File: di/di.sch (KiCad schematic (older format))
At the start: 35 parts

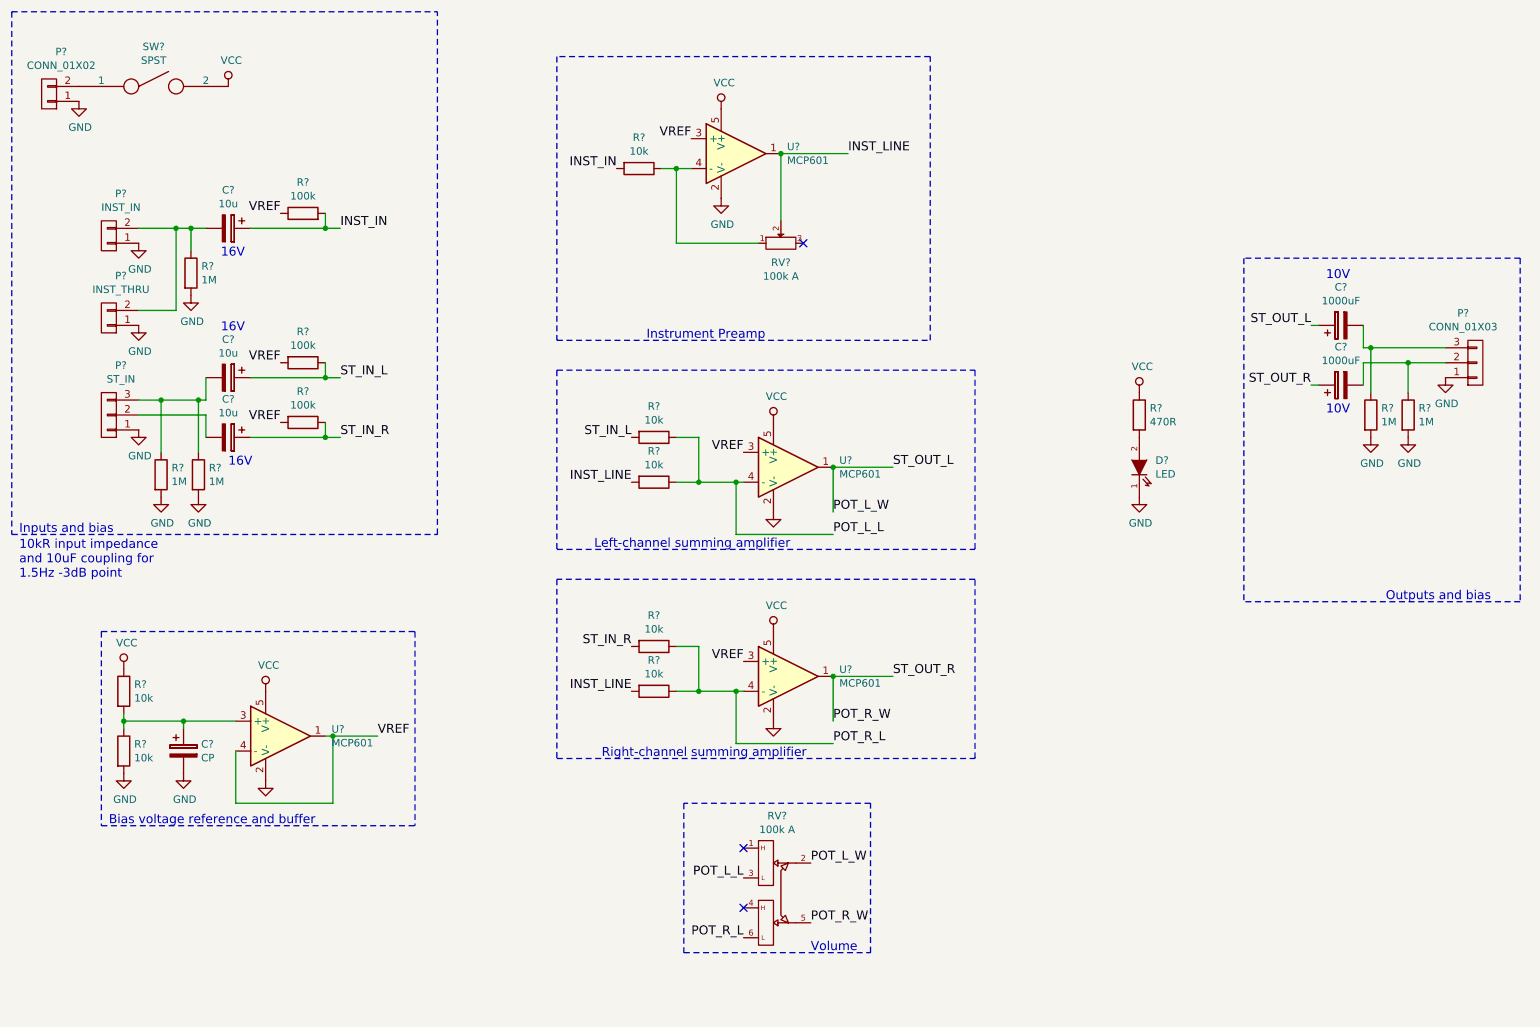
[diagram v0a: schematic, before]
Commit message: Higher impedance inst inputs
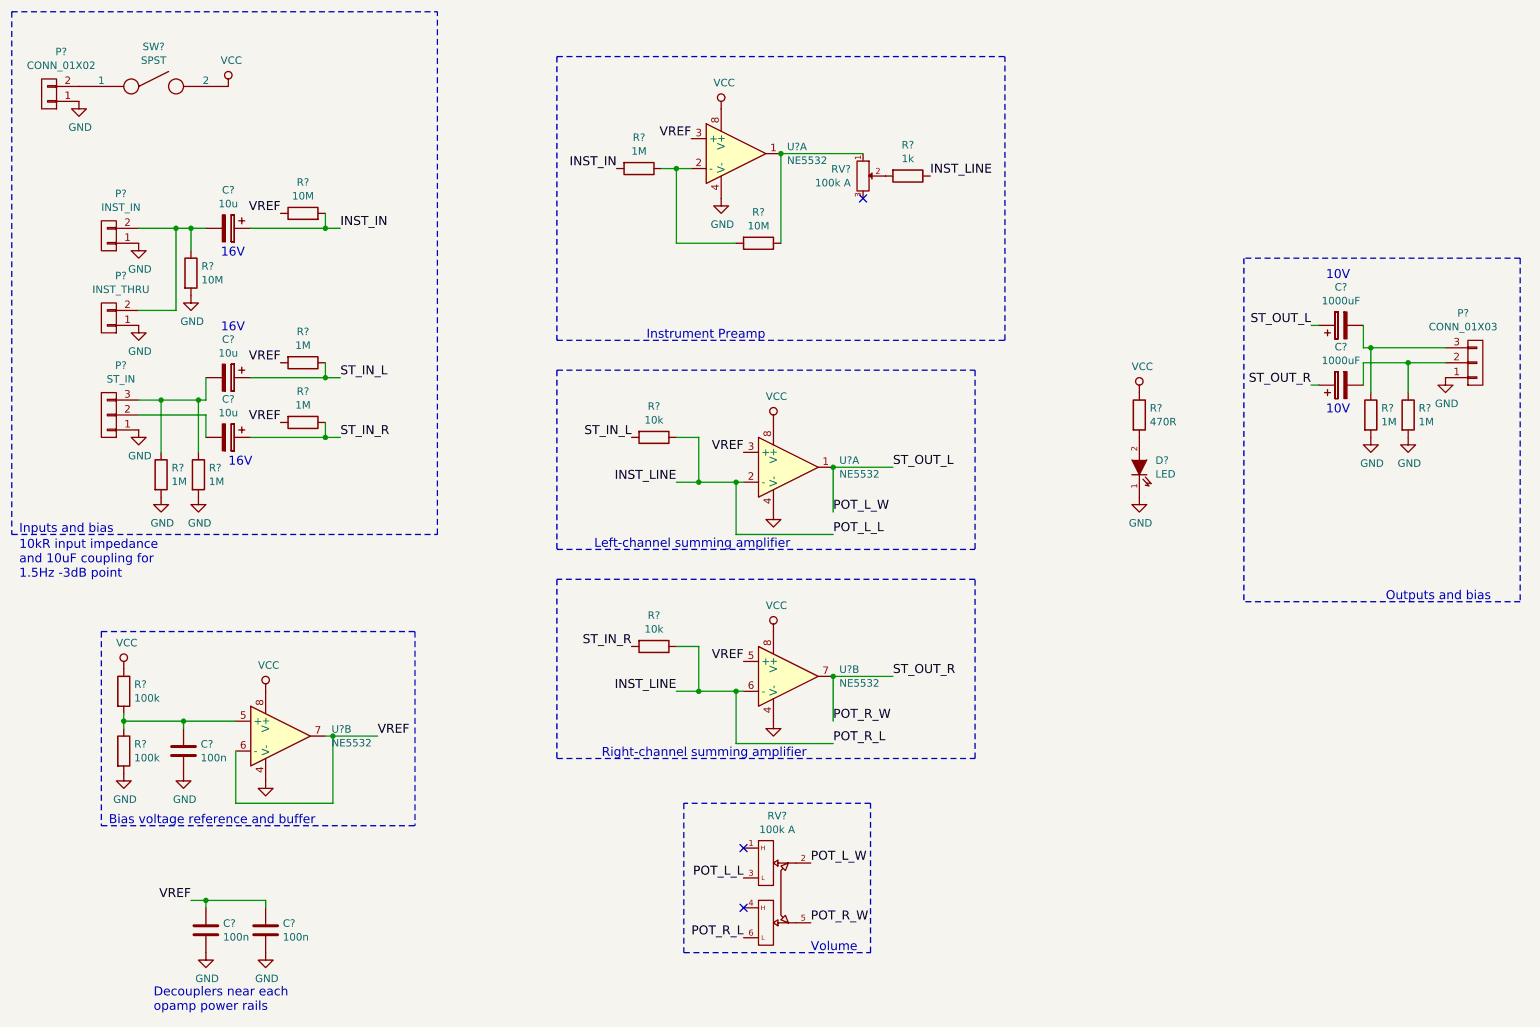
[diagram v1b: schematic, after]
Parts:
- removed C?: CP, symbol CP
- removed R? (x2): 10k, symbol R
- removed RV?: 100k A, symbol POT
- removed U? (x4): MCP601, symbol MCP601
- added C? (x3): 100n, symbol C
- added R?: 10M, symbol R
- added R?: 1k, symbol R
- added RV?: 100k A, symbol POT
- added U? (x4): NE5532, symbol NE5532
- R?: value 10k -> 1M
- R? (x2): value 10k -> 100k
- R?: value 100k -> 10M
- R? (x2): value 100k -> 1M
- R?: value 1M -> 10M
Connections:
- net POT_L_L is gone; now on net INST_LINE: R?.1, RV?.3
- net POT_R_L is gone; now on net INST_LINE: R?.1, RV?.6
- net GND: now also C?.2, C?.2, C?.2, U?.4 (V-), U?.4 (V-), U?.4 (V-), U?.4 (V-)
- net INST_LINE: now also R?.1, U?.2 (-), U?.6 (-)
- net POT_L_W: now also U?.1
- net POT_R_W: now also U?.7
- net VCC: now also U?.8 (V+), U?.8 (V+), U?.8 (V+), U?.8 (V+)
- net VREF: now also C?.1, C?.1, U?.3 (+), U?.3 (+), U?.5 (+), U?.6 (-), U?.7
- net at R?.1: now also R?.2, U?.2 (-)
- net at R?.1, R?.2: now also C?.1, U?.5 (+)
- new net: R?.1, RV?.1, U?.1
- new net: R?.2, RV?.2
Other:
- note added: "Decouplers near each\nopamp power rails"

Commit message: removed coupling from DI
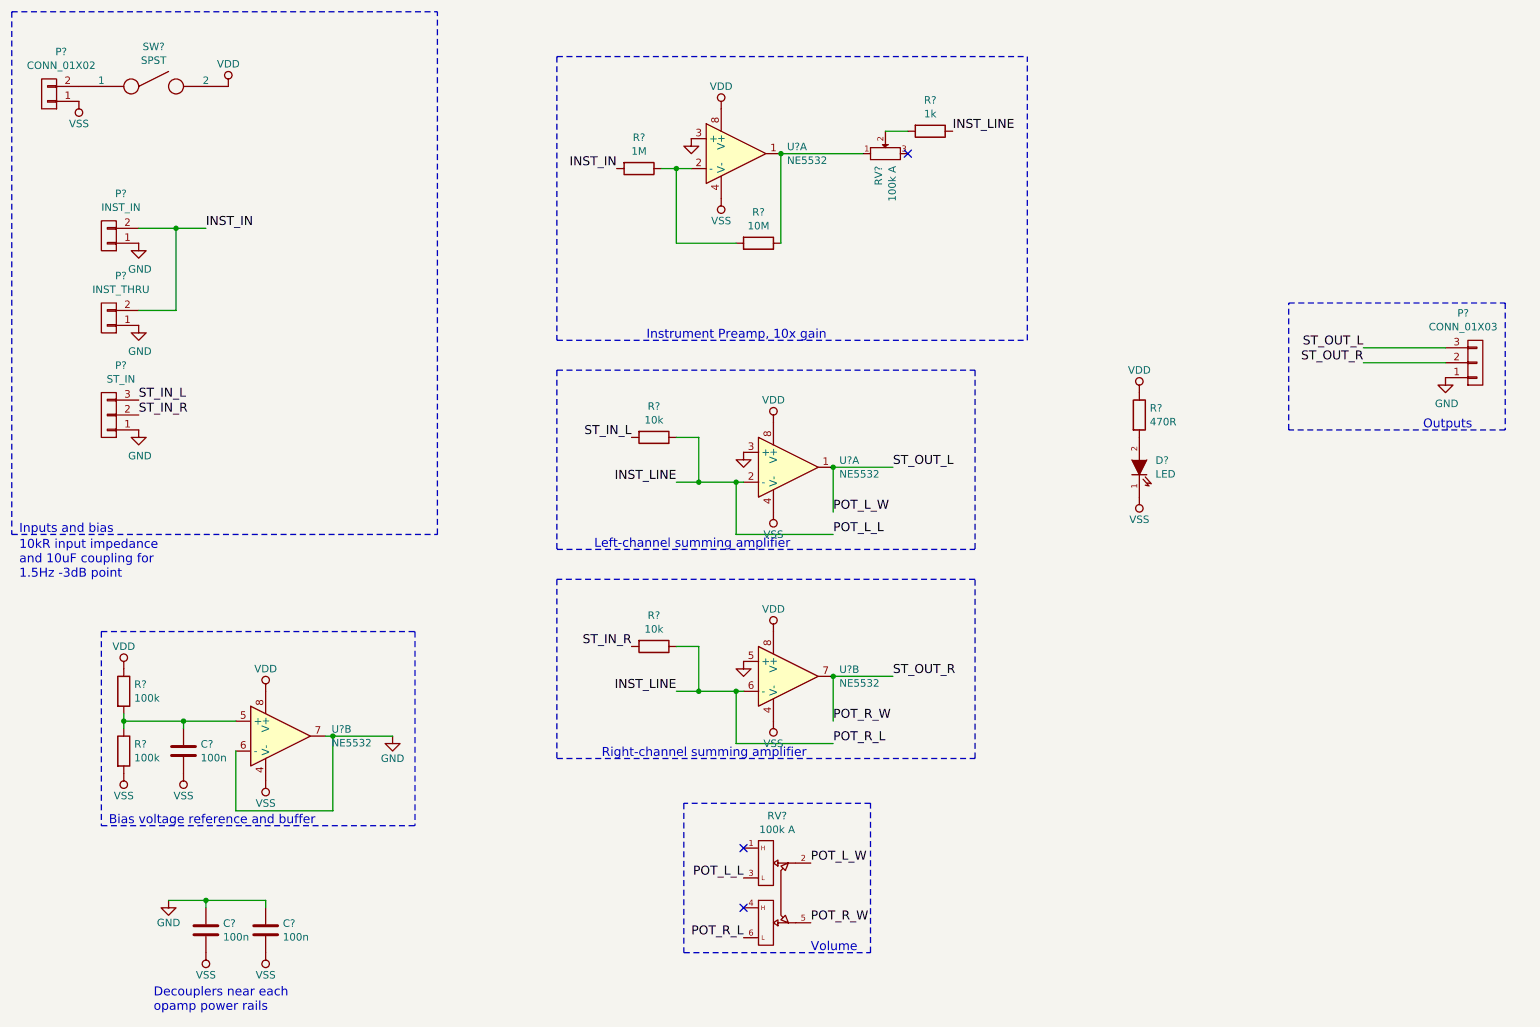
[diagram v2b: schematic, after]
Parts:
- removed C? (x3): 10u, symbol CP
- removed C? (x2): 1000uF, symbol CP
- removed R? (x2): 10M, symbol R
- removed R? (x6): 1M, symbol R
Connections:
- net VREF is gone; now on net GND: C?.1, C?.1, U?.3 (+), U?.3 (+), U?.5 (+), U?.6 (-), U?.7
- net GND: no longer C?.2, C?.2, C?.2, D?.1 (K), P?.1 (P1), R?.2, U?.4 (V-), U?.4 (V-), U?.4 (V-), U?.4 (V-)
- net INST_IN: now also P?.2 (P2), P?.2 (P2)
- net POT_L_W: now also P?.3 (P3)
- net POT_R_W: now also P?.2 (P2)
- net ST_IN_L: now also P?.3 (P3)
- net ST_IN_R: now also P?.2 (P2)
- net VCC renamed VDD
- new net VSS: C?.2, C?.2, C?.2, D?.1 (K), P?.1 (P1), R?.2, U?.4 (V-), U?.4 (V-), U?.4 (V-), U?.4 (V-)
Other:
- note added: "Instrument Preamp, 10x gain"
- note added: "Outputs"
- note removed: "10V"
- note removed: "16V"
- note removed: "Instrument Preamp"
- note removed: "Outputs and bias"
- moved on the sheet: R?, RV?

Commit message: Removed 10x gain from DI box
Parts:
- R?: value 10M -> 1M
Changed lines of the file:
@@
 P 5600 2250
 F 0 "R?" V 5392 2250 50  0000 C CNN
-F 1 "10M" V 5484 2250 50  0000 C CNN
+F 1 "1M" V 5484 2250 50  0000 C CNN
 F 2 "" V 5530 2250 50  0000 C CNN
 F 3 "" H 5600 2250 50  0000 C CNN

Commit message: Improved DI schematic
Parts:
- added R? (x2): 10k, symbol R
- added U? (x2): LM358, symbol LM358
- P?: value CONN_01X03 -> OUT
- RV?: value 100k A -> 10k A
- U? (x4): value NE5532 -> LM358
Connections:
- net GND: now also RV?.3, RV?.6
- net INST_LINE: now also R?.2, R?.2; no longer RV?.3, RV?.6
- net VDD: now also U?.8 (V+), U?.8 (V+)
- net VSS: now also U?.4 (V-), U?.4 (V-)
- net at RV?.1: now also U?.1, R?.1
- net at RV?.4: now also U?.7, R?.1
- removed net POT_L_W: P?.3 (P3), RV?.2, U?.1
- removed net POT_R_W: P?.2 (P2), RV?.5, U?.7
- new net: P?.2 (P2), U?.6 (-), U?.7
- new net: P?.3 (P3), U?.1, U?.2 (-)
- new net: RV?.2, U?.3 (+)
- new net: RV?.5, U?.5 (+)
- no-connect marks 3 -> 1
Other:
- note added: "Instrument Preamp, 1x gain"
- note added: "Left channel\noutput buffer"
- note added: "Right channel\noutput buffer"
- note added: "Stereo output"
- note added: "Stereo output\nvolume pot"
- note removed: "Instrument Preamp, 10x gain"
- note removed: "Outputs"
- note removed: "Volume"
- moved on the sheet: D?, P?, R?, RV?
